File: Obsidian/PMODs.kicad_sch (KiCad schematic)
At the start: 6 parts, among them J14 Conn_02x06_Top_Bottom, J15 Conn_02x06_Top_Bottom, J4 Conn_02x06_Top_Bottom, J5 Conn_02x06_Top_Bottom, J6 Conn_02x06_Top_Bottom, J7 Conn_02x06_Top_Bottom

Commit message: revison v1.1.0 ready to review
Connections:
- net PMOD1_0 renamed PMOD1_1_P
- net PMOD1_1 renamed PMOD1_1_N
- net PMOD1_2 renamed PMOD1_2_P
- net PMOD1_3 renamed PMOD1_2_N
- net PMOD1_4 renamed PMOD1_3_P
- net PMOD1_5 renamed PMOD1_3_N
- net PMOD1_6 renamed PMOD1_4_P
- net PMOD1_7 renamed PMOD1_4_N
- net PMOD2_0 renamed PMOD2_1_P
- net PMOD2_1 renamed PMOD2_1_N
- net PMOD2_2 renamed PMOD2_2_P
- net PMOD2_3 renamed PMOD2_2_N
- net PMOD2_4 renamed PMOD2_3_P
- net PMOD2_5 renamed PMOD2_3_N
- net PMOD2_6 renamed PMOD2_4_P
- net PMOD2_7 renamed PMOD2_4_N
- net PMOD3_0 renamed PMOD3_1_P
- net PMOD3_1 renamed PMOD3_1_N
- net PMOD3_2 renamed PMOD3_2_P
- net PMOD3_3 renamed PMOD3_2_N
- net PMOD3_4 renamed PMOD3_3_P
- net PMOD3_5 renamed PMOD3_3_N
- net PMOD3_6 renamed PMOD3_4_P
- net PMOD3_7 renamed PMOD3_4_N
- net PMOD4_0 renamed PMOD4_1_P
- net PMOD4_1 renamed PMOD4_1_N
- net PMOD4_2 renamed PMOD4_2_P
- net PMOD4_3 renamed PMOD4_2_N
- net PMOD4_4 renamed PMOD4_3_P
- net PMOD4_5 renamed PMOD4_3_N
- net PMOD4_6 renamed PMOD4_4_P
- net PMOD4_7 renamed PMOD4_4_N

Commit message: minor changes
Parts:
- added J17: Micro_SD_Card, Connector_Card:microSD_HC_Molex_47219-2001, symbol Connector:Micro_SD_Card
- added R105, R106, R107, R108, R109, R110: R0402_10K_1%_0.0625W_100PPM, Resistors SMD:RESC1005X40N, symbol Resistors SMD:R0402_10K_1%_0.0625W_100PPM
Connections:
- net GND: now also J17.6 (VSS), J17.9 (SHIELD)
- net PMOD6_0: now also J17.2 (DAT3/CD), R106.2
- net PMOD6_1: now also J17.3 (CMD), R107.2
- net PMOD6_2: now also J17.7 (DAT0), R109.2
- net PMOD6_3: now also J17.5 (CLK), R108.2
- net PMOD6_4: now also J17.8 (DAT1), R110.2
- net PMOD6_5: now also J17.1 (DAT2), R105.2
- new net +3V3: J17.4 (VDD), R105.1, R106.1, R107.1, R108.1, R109.1, R110.1
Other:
- moved on the sheet: J14, J15, J4, J5, J6, J7

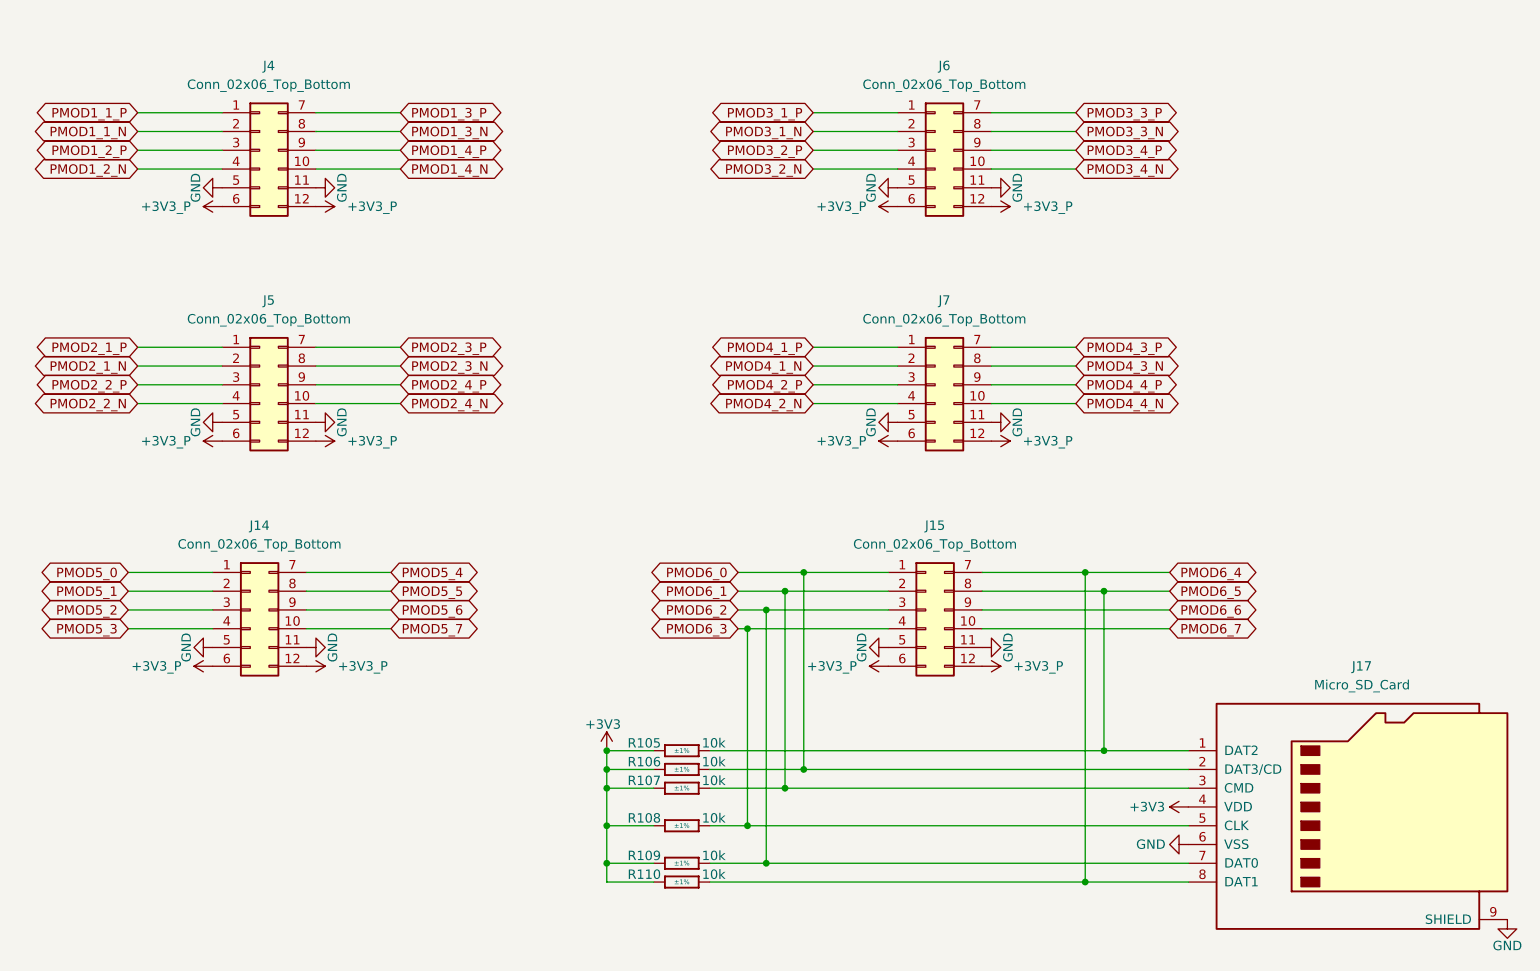
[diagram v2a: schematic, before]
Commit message: new font; removed clk gen; added resistors for 2 PMODs
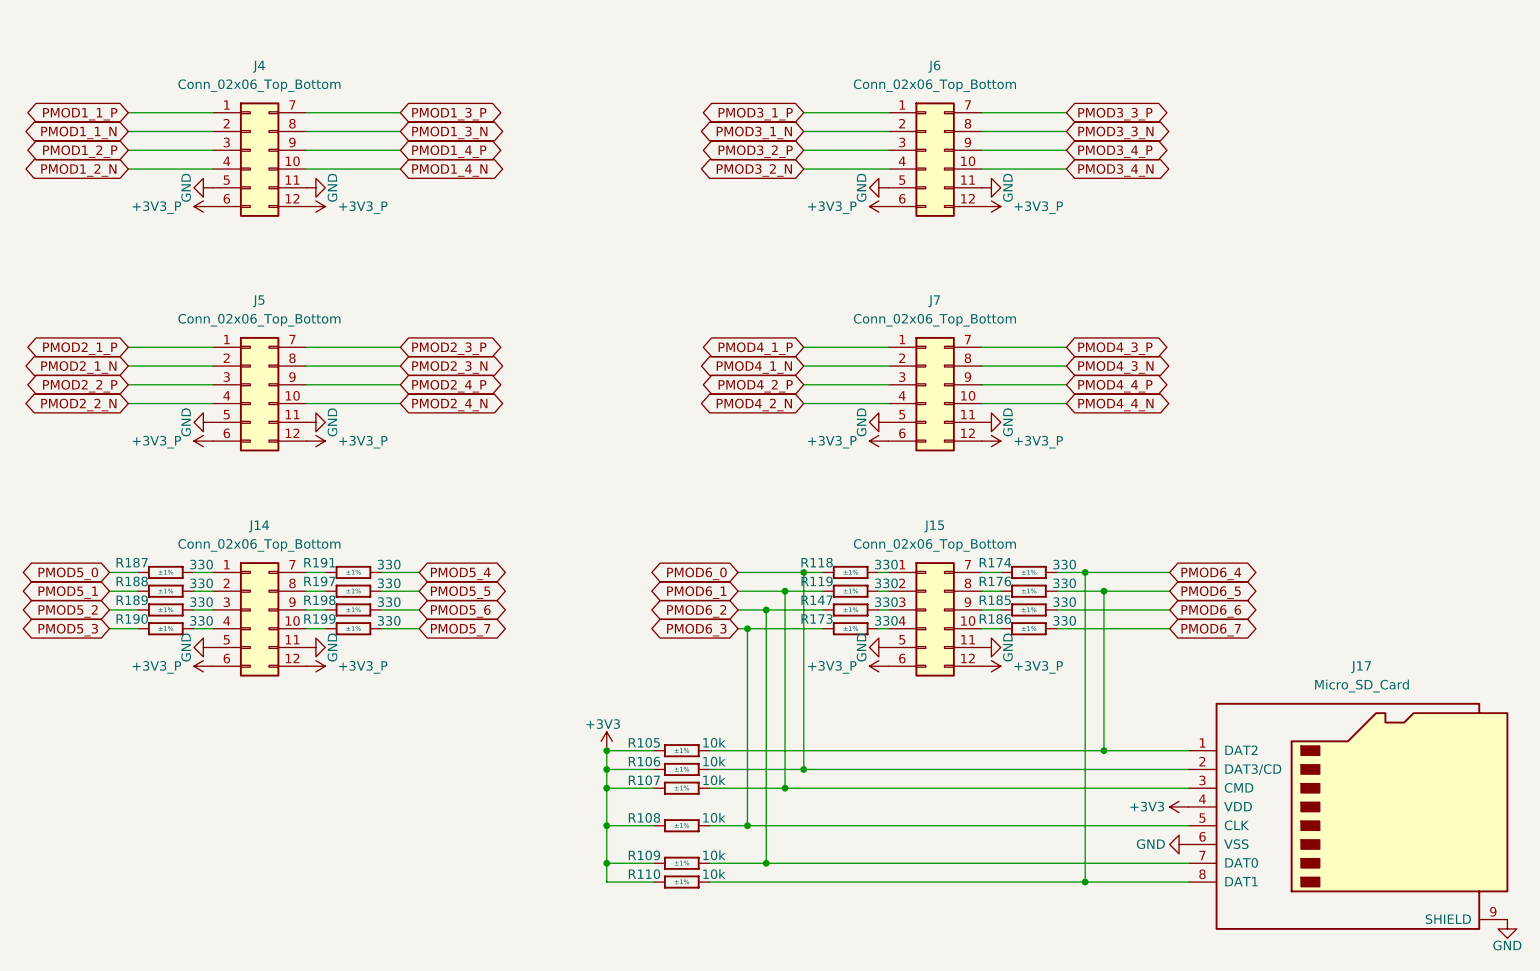
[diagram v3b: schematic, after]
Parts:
- added R118, R119, R147, R173, R174, R176, R185, R186, R187, R188, R189, R190, R191, R197, R198, R199: R0402_330R_1%_0.0625W_100PPM, Resistors SMD:RESC1005X40N, symbol Resistors SMD:R0402_330R_1%_0.0625W_100PPM
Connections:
- net PMOD5_0: now also R187.1; no longer J14.1 (Pin_1)
- net PMOD5_1: now also R188.1; no longer J14.2 (Pin_2)
- net PMOD5_2: now also R189.1; no longer J14.3 (Pin_3)
- net PMOD5_3: now also R190.1; no longer J14.4 (Pin_4)
- net PMOD5_4: now also R191.2; no longer J14.7 (Pin_7)
- net PMOD5_5: now also R197.2; no longer J14.8 (Pin_8)
- net PMOD5_6: now also R198.2; no longer J14.9 (Pin_9)
- net PMOD5_7: now also R199.2; no longer J14.10 (Pin_10)
- net PMOD6_0: now also R118.1; no longer J15.1 (Pin_1)
- net PMOD6_1: now also R119.1; no longer J15.2 (Pin_2)
- net PMOD6_2: now also R147.1; no longer J15.3 (Pin_3)
- net PMOD6_3: now also R173.1; no longer J15.4 (Pin_4)
- net PMOD6_4: now also R174.2; no longer J15.7 (Pin_7)
- net PMOD6_5: now also R176.2; no longer J15.8 (Pin_8)
- net PMOD6_6: now also R185.2; no longer J15.9 (Pin_9)
- net PMOD6_7: now also R186.2; no longer J15.10 (Pin_10)
- new net: J15.8 (Pin_8), R176.1
- new net: J14.1 (Pin_1), R187.2
- new net: J15.2 (Pin_2), R119.2
- new net: J14.2 (Pin_2), R188.2
- new net: J14.10 (Pin_10), R199.1
- new net: J15.9 (Pin_9), R185.1
- new net: J14.3 (Pin_3), R189.2
- new net: J14.4 (Pin_4), R190.2
- new net: J14.7 (Pin_7), R191.1
- new net: J14.8 (Pin_8), R197.1
- new net: J14.9 (Pin_9), R198.1
- new net: J15.1 (Pin_1), R118.2
- new net: J15.10 (Pin_10), R186.1
- new net: J15.3 (Pin_3), R147.2
- new net: J15.4 (Pin_4), R173.2
- new net: J15.7 (Pin_7), R174.1
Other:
- moved on the sheet: J4, J5, J6, J7

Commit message: ready to manufacture
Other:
- note added: "PMOD A"
- note added: "PMOD B"
- note added: "PMOD C"
- note added: "PMOD D"
- note added: "PMOD E"
- note added: "PMOD F"
